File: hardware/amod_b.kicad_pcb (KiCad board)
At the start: 4 copper layers, 100 x 100 mm, 147 parts, among them J1001 SMA, J1002 SMA, J101 USB-C, J102 rails, J1101 SMA, J1201 SMA, J201 SMA, J202 5-12V, J301 SMA, J302 SMA, J303 SMA, J304 motor, J305 Pmod, J401 SMA, J402 SMA, J701 SMA, J801 SMA, J802 piezo, J901 SMA, Q301 AO3401A, SW301 ON, U1001 OPA810, U1002 OPA810, U101 LM2664, U102 3.3V, U1101 INA240, U1102 OPA810, U1201 INA181, U1202 OPA810, U301 DRV8311H, U302 TLV3501, U401 OPA2171, U501 MT6701, U502 DRV5055, U503 DRV5055, U504 QRE1113, U601 LSM6DSO, U602 74LVC1G125, U701 OPA810, U801 OPA810, U901 OPA810

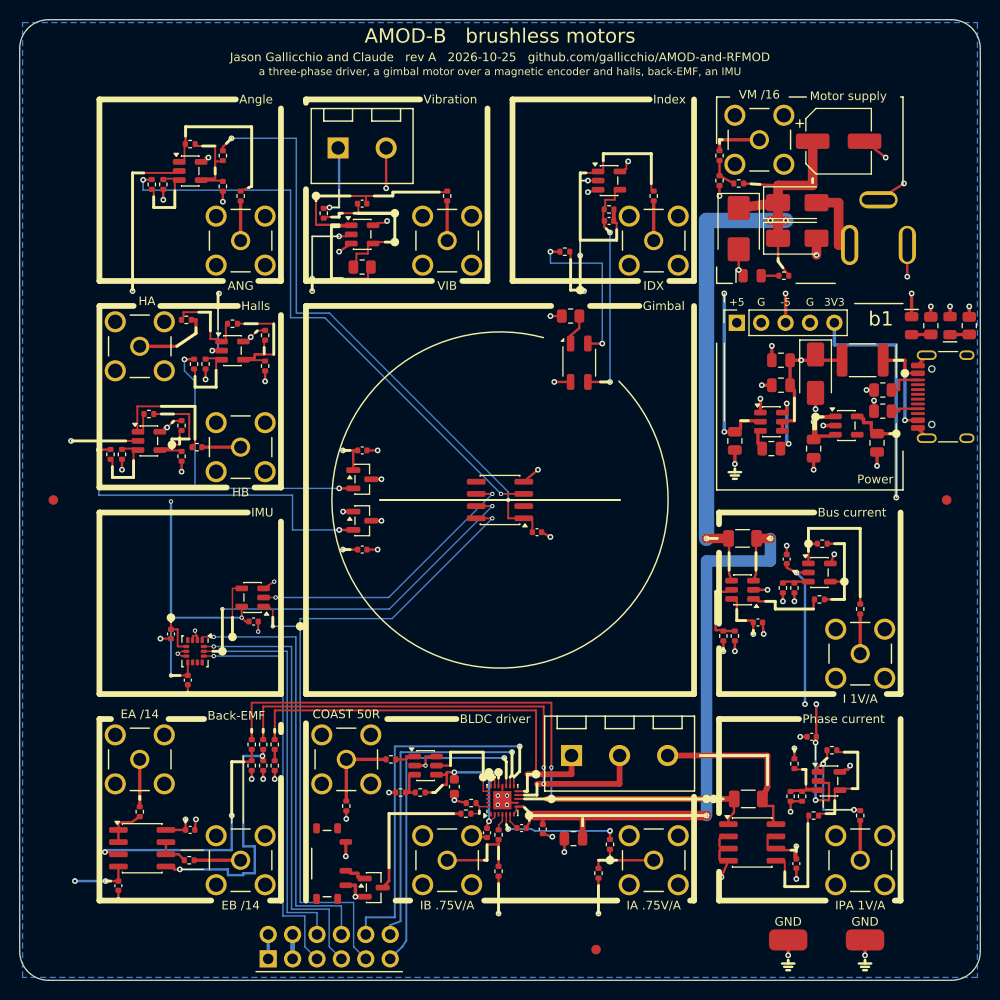
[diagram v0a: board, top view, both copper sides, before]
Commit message: Pre-order checks from CLAUDE_PCB.md's new lessons (Prompt 21): the KF301 terminals turned for their wire openings (CPL +180, body 3.7 / 4.0, a wire-face check), four oversold parts swapped (27R, 6.8k, 220n, OPA847IDBVT at its own +180), fourteen vias moved out of SMD pads (check_layout.py gates it and RF detours), 200-250 mW terminations, assembly drawings from Fab and silk fitted to Letter (fit_pdf.py from CostasLink), the stock gate on JLCPCB's free count, electrolytics in the rotation check, the RF gates surveyed (rf_extract.py, rf_survey.py) and written into the DOA lists; all nine boards rebuilt: ERC 0, DRC 0, every check
Co-Authored-By: Claude Opus 5.5 <noreply@anthropic.com>
Claude-Session: https://claude.ai/code/session_01RKeoKvFFzjk3cEBLCXXHnB
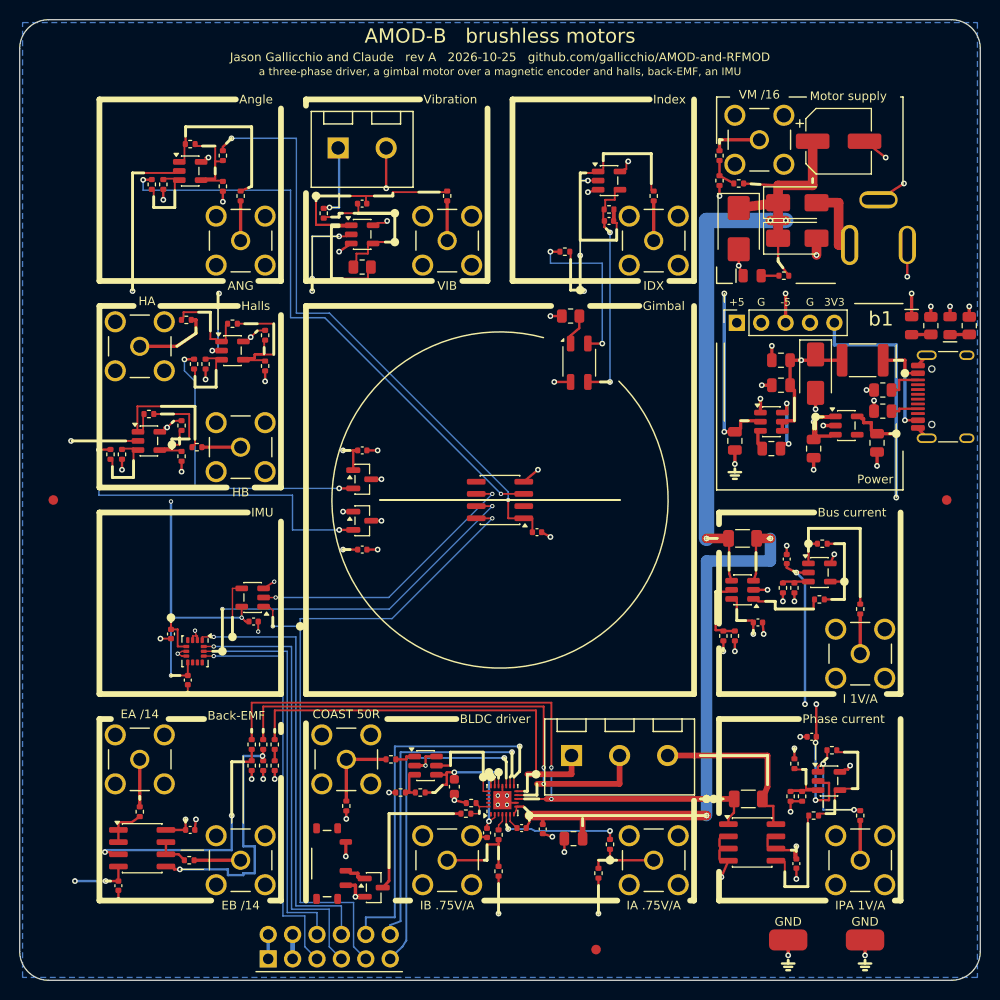
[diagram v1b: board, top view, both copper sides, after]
